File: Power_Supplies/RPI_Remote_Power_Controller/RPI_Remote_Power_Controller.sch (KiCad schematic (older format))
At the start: 25 parts, among them J1 Screw_Terminal_01x02, J10 Screw_Terminal_01x03, J11 Raspberry_Pi_Zero_W, J12 Screw_Terminal_01x02, J2 Screw_Terminal_01x02, J3 Screw_Terminal_01x02, J4 Screw_Terminal_01x02, J5 Screw_Terminal_01x02, J6 Screw_Terminal_01x02, J7 Screw_Terminal_01x02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

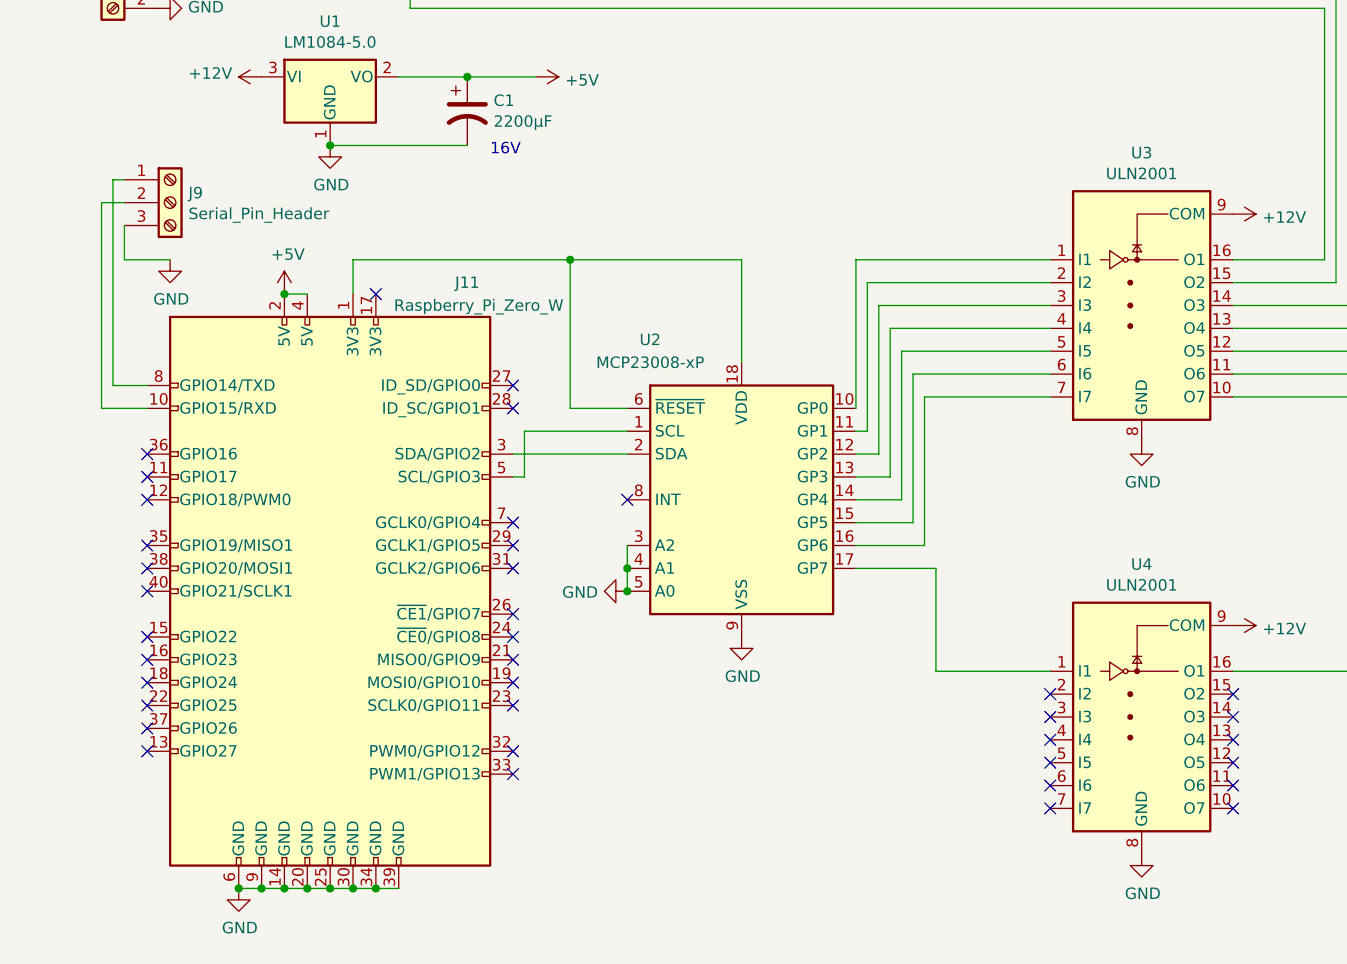
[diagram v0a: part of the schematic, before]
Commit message: - We really are using ULN2003s. - Connect the ~RESET line of the MCP23008 to pin 40 of the GPIO   header.
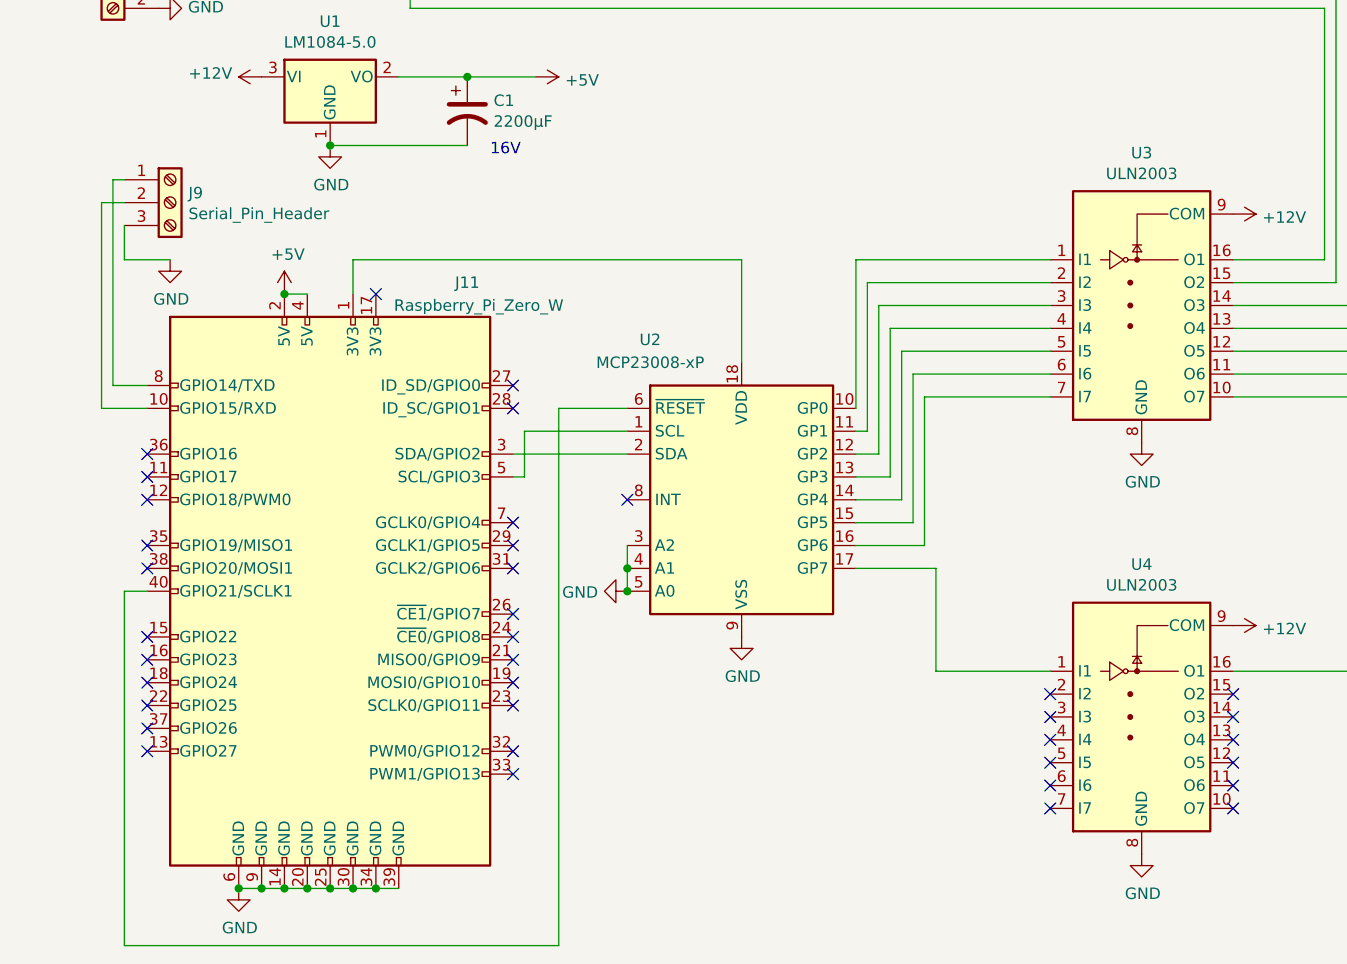
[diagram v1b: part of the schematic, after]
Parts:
- U3, U4: value ULN2001 -> ULN2003
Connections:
- net at J11.1 (3V3), U2.18 (VDD): no longer U2.6 (~RESET)
- net at J11.40 (GPIO21/SCLK1): now also U2.6 (~RESET)
- no-connect marks 38 -> 37
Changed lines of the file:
@@
 P 5400 9050
 F 0 "U4" H 5400 9717 50  0000 C CNN
-F 1 "ULN2001" H 5400 9626 50  0000 C CNN
+F 1 "ULN2003" H 5400 9626 50  0000 C CNN
 F 2 "Package_DIP:DIP-16_W7.62mm_Socket" H 5450 8500 50  0001 L CNN
 F 3 "http://www.ti.com/lit/ds/symlink/uln2003a.pdf" H 5500 8850 50  0001 C CNN
@@
 P 5400 7250
 F 0 "U3" H 5400 7917 50  0000 C CNN
-F 1 "ULN2001" H 5400 7826 50  0000 C CNN
+F 1 "ULN2003" H 5400 7826 50  0000 C CNN
 F 2 "Package_DIP:DIP-16_W7.62mm_Socket" H 5450 6700 50  0001 L CNN
 F 3 "http://www.ti.com/lit/ds/symlink/uln2003a.pdf" H 5500 7050 50  0001 C CNN
@@
 	1950 7200 1950 7050
 Wire Wire Line
-	1950 7050 2900 7050
-Wire Wire Line
 	3650 7050 3650 7500
 NoConn ~ 3150 8100
@@
 $EndComp
 Connection ~ 3150 8500
-Wire Wire Line
-	3150 7700 2900 7700
-Wire Wire Line
-	2900 7700 2900 7050
-Connection ~ 2900 7050
-Wire Wire Line
-	2900 7050 3650 7050
 Text GLabel 1450 950  2    50   Output ~ 0
 Mains_Hot
@@
 NoConn ~ 1050 8300
 NoConn ~ 1050 8400
-NoConn ~ 1050 8500
 NoConn ~ 1050 8700
 NoConn ~ 1050 8800
@@
 	0    -1   -1   0
 $EndComp
+Wire Wire Line
+	1950 7050 3650 7050
+Wire Wire Line
+	1050 8500 950  8500
+Wire Wire Line
+	950  8500 950  10050
+Wire Wire Line
+	950  10050 2850 10050
+Wire Wire Line
+	2850 10050 2850 7700
+Wire Wire Line
+	2850 7700 3150 7700
 $EndSCHEMATC
